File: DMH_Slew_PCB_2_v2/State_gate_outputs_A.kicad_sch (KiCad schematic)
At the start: 26 parts, among them J4 TS_Jack_6.35mm_Sw, J5 TS_Jack_6.35mm_Sw, J51 Conn_01x08_PinHeader, Q5 BC548, Q6 BC548, U1 TL074

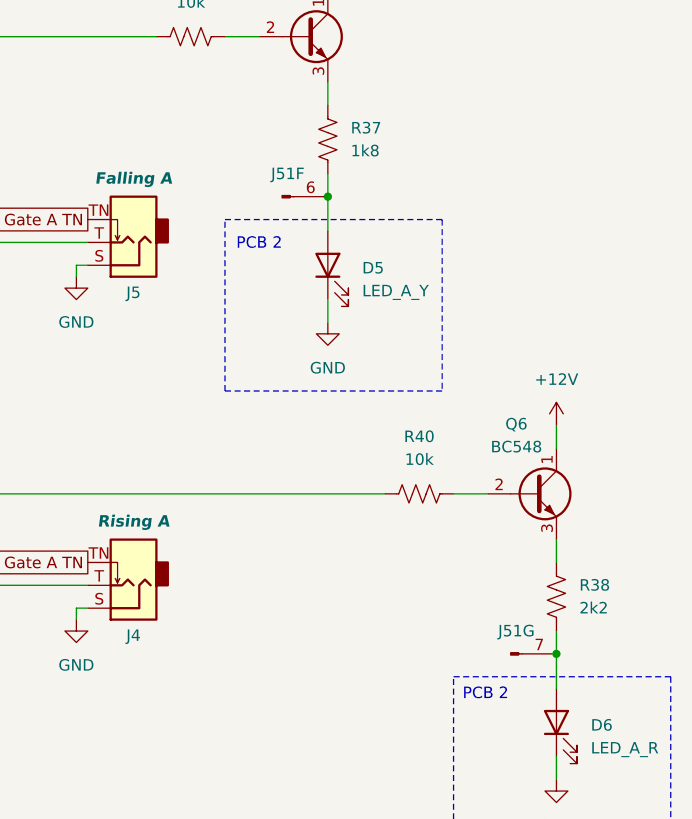
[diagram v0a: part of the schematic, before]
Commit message: PCB 2 component placement done
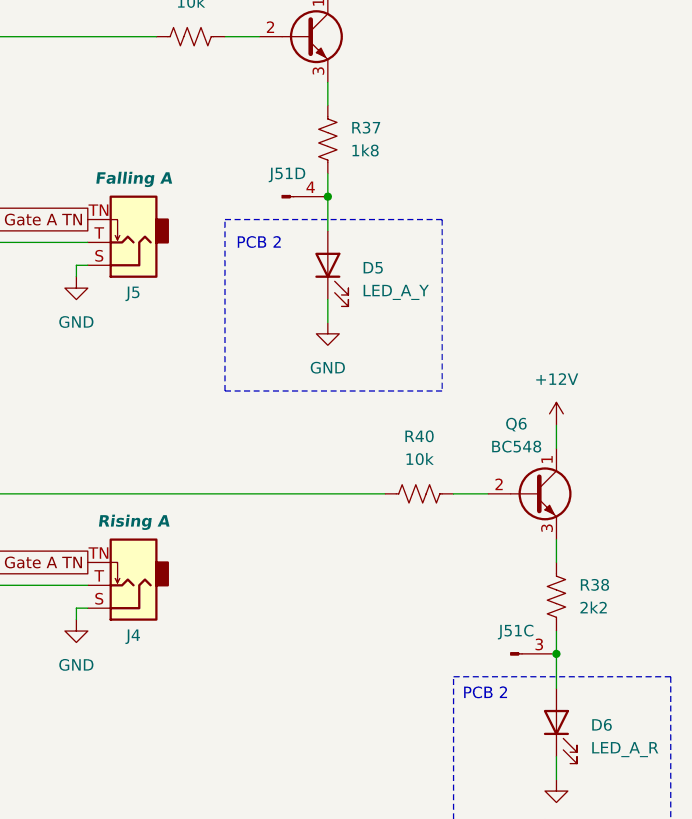
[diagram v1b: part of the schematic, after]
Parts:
- J51: footprint Connector_PinHeader_2.54mm:PinHeader_1x08_P2.54mm_Vertical -> Connector_PinSocket_2.54mm:PinSocket_1x08_P2.54mm_Vertical
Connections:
- net at D6.2 (A), R38.2: now also J51.3 (Pin_3); no longer J51.7 (Pin_7)
- net at D5.2 (A), R37.2: now also J51.4 (Pin_4); no longer J51.6 (Pin_6)
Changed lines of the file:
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@@
 		(lib_id "SynthStuff:Conn_01x08_PinHeader")
 		(at 251.46 106.68 0)
-		(unit 7)
+		(unit 3)
 		(exclude_from_sim no)
 		(in_bom yes)
@@
 			)
 		)
-		(property "Footprint" "Connector_PinHeader_2.54mm:PinHeader_1x08_P2.54mm_Vertical"
+		(property "Footprint" "Connector_PinSocket_2.54mm:PinSocket_1x08_P2.54mm_Vertical"
 			(at 251.46 106.68 0)
 			(effects
@@
 			)
 		)
+		(property "Function" ""
+			(at 251.46 106.68 0)
+			(effects
+				(font
+					(size 1.27 1.27)
+				)
+			)
+		)
 		(pin "3"
 		)
@@
 				(path "/58f4306d-5387-4983-bb08-41a2313fd315/695faa68-e325-44bd-a237-dc69a864c9b9"
 					(reference "J51")
-					(unit 7)
+					(unit 3)
 				)
 			)
@@
 		(lib_id "SynthStuff:Conn_01x08_PinHeader")
 		(at 226.06 55.88 0)
-		(unit 6)
+		(unit 4)
 		(exclude_from_sim no)
 		(in_bom yes)
@@
 			)
 		)
-		(property "Footprint" "Connector_PinHeader_2.54mm:PinHeader_1x08_P2.54mm_Vertical"
+		(property "Footprint" "Connector_PinSocket_2.54mm:PinSocket_1x08_P2.54mm_Vertical"
 			(at 226.06 55.88 0)
 			(effects
@@
 			)
 		)
+		(property "Function" ""
+			(at 226.06 55.88 0)
+			(effects
+				(font
+					(size 1.27 1.27)
+				)
+			)
+		)
 		(pin "3"
 		)
@@
 				(path "/58f4306d-5387-4983-bb08-41a2313fd315/695faa68-e325-44bd-a237-dc69a864c9b9"
 					(reference "J51")
-					(unit 6)
-				)
-			)
+					(unit 4)
+				)
+			)
